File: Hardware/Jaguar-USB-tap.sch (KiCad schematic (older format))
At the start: 24 parts, among them J1 DB15, P1 CONN_01X03, P2 USB_B, P3 CONN_01X05, U1 NCP1117ST33T3G, U2 STM32F070F6, U3 TXB0106, U4 TXB0106, Y1 8MHz

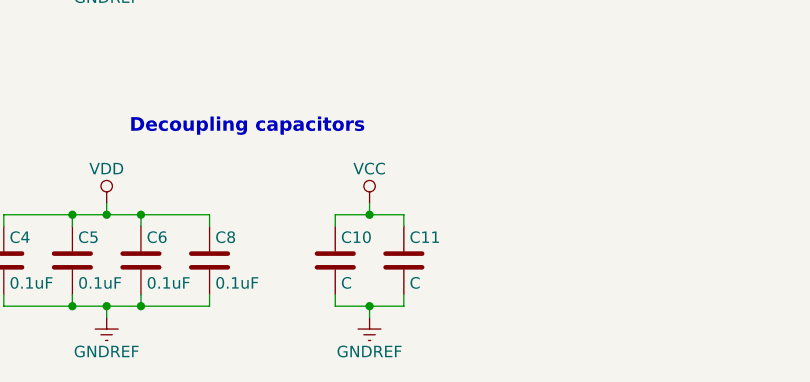
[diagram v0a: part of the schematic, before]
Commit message: Add a preview image for casual inspection.
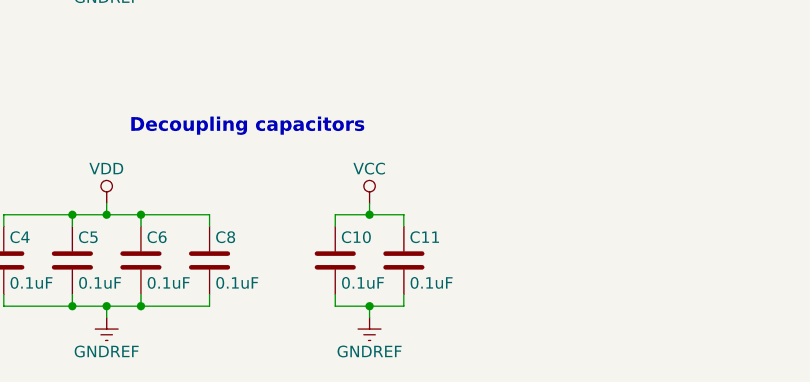
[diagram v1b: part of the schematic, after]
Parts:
- C10, C11: value C -> 0.1uF
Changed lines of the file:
@@
 P 4500 7100
 F 0 "C10" H 4525 7200 50  0000 L CNN
-F 1 "C" H 4525 7000 50  0000 L CNN
+F 1 "0.1uF" H 4525 7000 50  0000 L CNN
 F 2 "" H 4538 6950 50  0000 C CNN
 F 3 "" H 4500 7100 50  0000 C CNN
@@
 P 4800 7100
 F 0 "C11" H 4825 7200 50  0000 L CNN
-F 1 "C" H 4825 7000 50  0000 L CNN
+F 1 "0.1uF" H 4825 7000 50  0000 L CNN
 F 2 "" H 4838 6950 50  0000 C CNN
 F 3 "" H 4800 7100 50  0000 C CNN

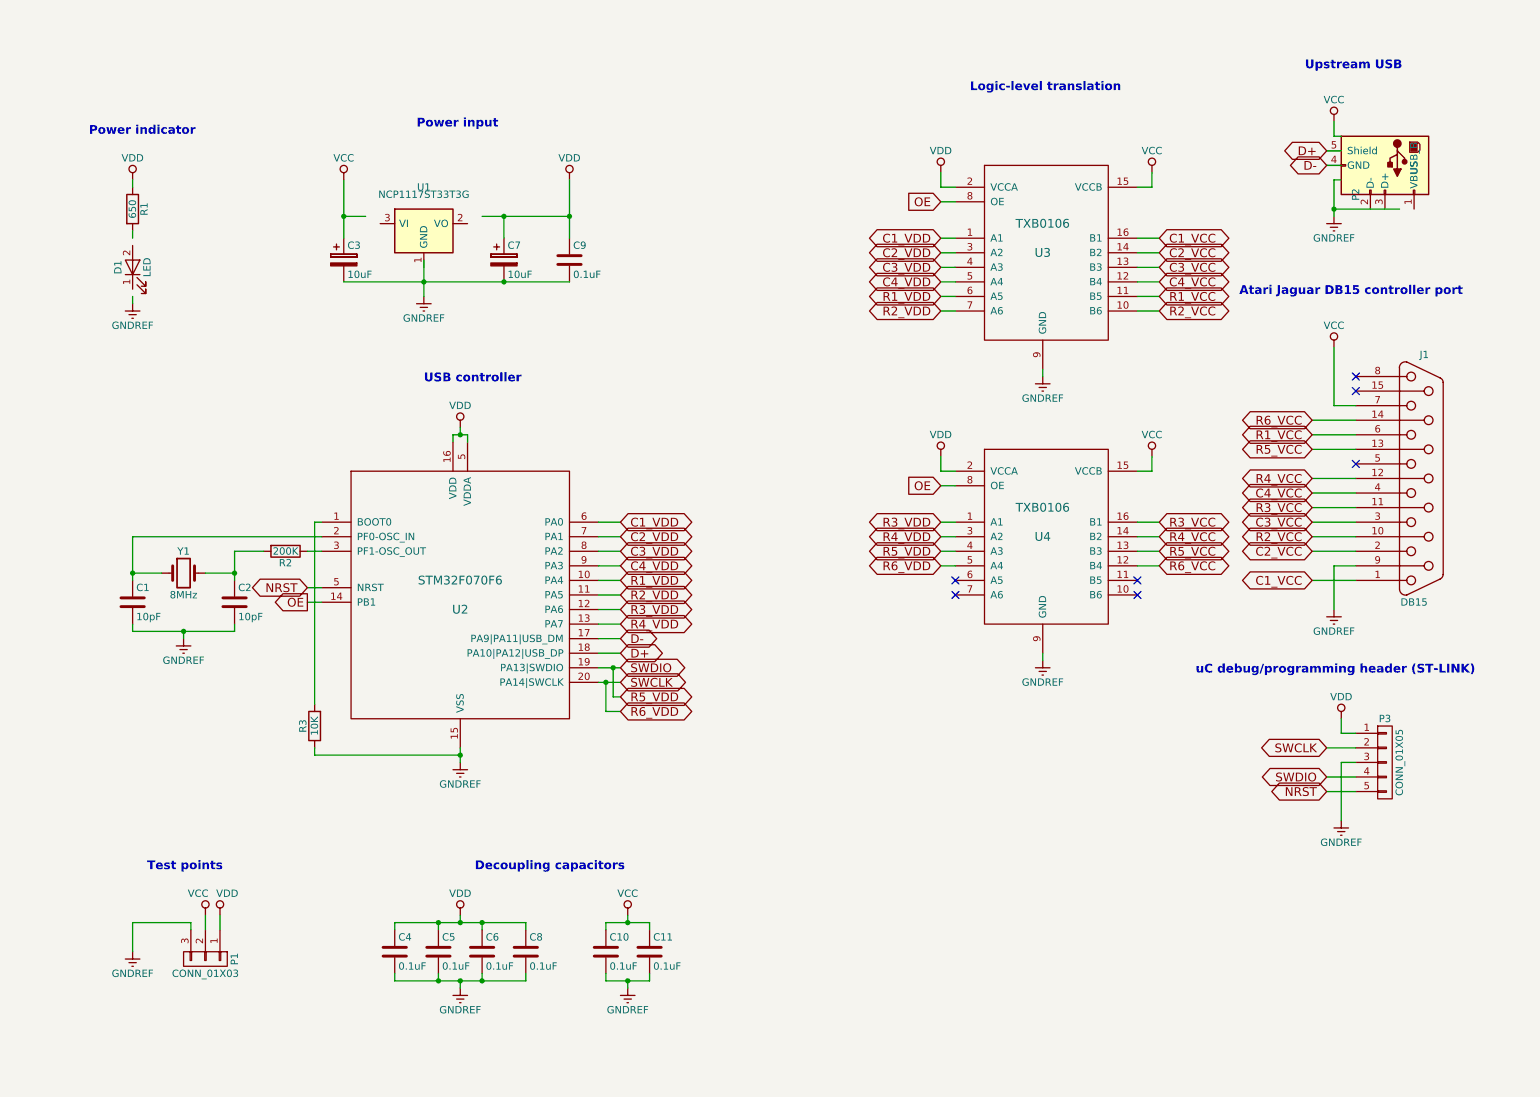
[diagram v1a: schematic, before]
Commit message: Add PCB work.
1) Add footprints for TSSOP16 and TSSOP20 devices.
2) Create a PCB layout for adapter and board cut.
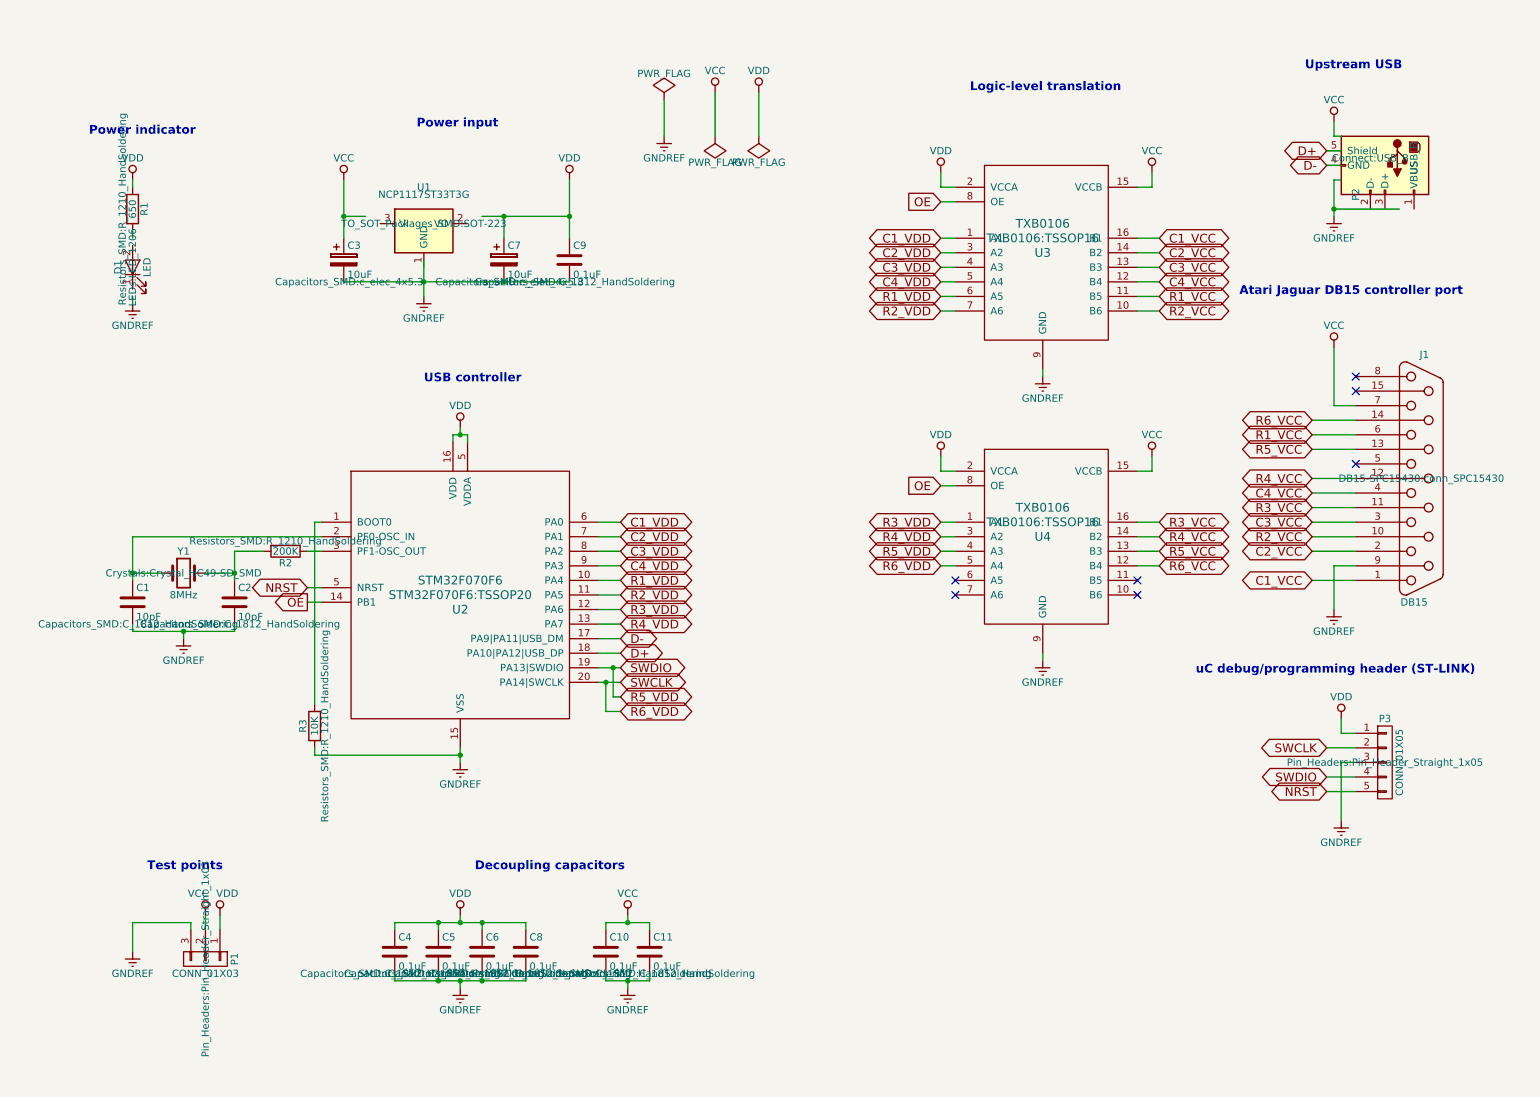
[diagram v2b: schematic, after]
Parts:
- C1, C10, C11, C2, C4, C5, C6, C8, C9: footprint (none) -> Capacitors_SMD:C_1812_HandSoldering
- C3, C7: footprint (none) -> Capacitors_SMD:c_elec_4x5.3
- D1: footprint (none) -> LEDs:LED_1206
- J1: footprint (none) -> DB15-SPC15430:conn_SPC15430
- P1: footprint (none) -> Pin_Headers:Pin_Header_Straight_1x03
- P2: footprint (none) -> Connect:USB_B
- P3: footprint (none) -> Pin_Headers:Pin_Header_Straight_1x05
- R1, R2, R3: footprint (none) -> Resistors_SMD:R_1210_HandSoldering
- U1: footprint (none) -> TO_SOT_Packages_SMD:SOT-223
- U2: footprint (none) -> STM32F070F6:TSSOP20
- U3, U4: footprint (none) -> TXB0106:TSSOP16
- Y1: footprint (none) -> Crystals:Crystal_HC49-SD_SMD
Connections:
- wire segments 133 -> 136
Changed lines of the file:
@@
 F 0 "U2" H 3500 4550 60  0000 C CNN
 F 1 "STM32F070F6" H 3500 4750 60  0000 C CNN
-F 2 "" H 3500 4650 60  0000 C CNN
+F 2 "STM32F070F6:TSSOP20" H 3500 4650 60  0000 C CNN
 F 3 "" H 3500 4650 60  0000 C CNN
 	1    3500 4650
@@
 F 0 "P2" H 10050 1500 50  0000 C CNN
 F 1 "USB_B" H 9800 1900 50  0000 C CNN
-F 2 "" V 9800 1600 50  0000 C CNN
+F 2 "Connect:USB_B" V 9800 1600 50  0000 C CNN
 F 3 "" V 9800 1600 50  0000 C CNN
 	1    9850 1700
@@
 F 0 "P3" H 9850 6100 50  0000 C CNN
 F 1 "CONN_01X05" V 9950 5800 50  0000 C CNN
-F 2 "" H 9850 5800 50  0000 C CNN
+F 2 "Pin_Headers:Pin_Header_Straight_1x05" H 9850 5800 50  0000 C CNN
 F 3 "" H 9850 5800 50  0000 C CNN
 	1    9850 5800
@@
 F 0 "R1" V 1330 2000 50  0000 C CNN
 F 1 "650" V 1250 2000 50  0000 C CNN
-F 2 "" V 1180 2000 50  0000 C CNN
+F 2 "Resistors_SMD:R_1210_HandSoldering" V 1180 2000 50  0000 C CNN
 F 3 "" H 1250 2000 50  0000 C CNN
 	1    1250 2000
@@
 F 0 "D1" H 1250 2500 50  0000 C CNN
 F 1 "LED" H 1250 2300 50  0000 C CNN
-F 2 "" H 1250 2400 50  0000 C CNN
+F 2 "LEDs:LED_1206" H 1250 2400 50  0000 C CNN
 F 3 "" H 1250 2400 50  0000 C CNN
 	1    1250 2400
@@
 F 0 "U1" H 3250 2350 50  0000 C CNN
 F 1 "NCP1117ST33T3G" H 3250 2300 50  0000 C CNN
-F 2 "" H 3250 2100 50  0000 C CNN
+F 2 "TO_SOT_Packages_SMD:SOT-223" H 3250 2100 50  0000 C CNN
 F 3 "" H 3250 2100 50  0000 C CNN
 	1    3250 2100
@@
 F 0 "C3" H 2725 2450 50  0000 L CNN
 F 1 "10uF" H 2725 2250 50  0000 L CNN
-F 2 "" H 2738 2200 50  0000 C CNN
+F 2 "Capacitors_SMD:c_elec_4x5.3" H 2738 2200 50  0000 C CNN
 F 3 "" H 2700 2350 50  0000 C CNN
 	1    2700 2350
@@
 F 0 "C7" H 3825 2450 50  0000 L CNN
 F 1 "10uF" H 3825 2250 50  0000 L CNN
-F 2 "" H 3838 2200 50  0000 C CNN
+F 2 "Capacitors_SMD:c_elec_4x5.3" H 3838 2200 50  0000 C CNN
 F 3 "" H 3800 2350 50  0000 C CNN
 	1    3800 2350
@@
 F 0 "C9" H 4275 2450 50  0000 L CNN
 F 1 "0.1uF" H 4275 2250 50  0000 L CNN
-F 2 "" H 4288 2200 50  0000 C CNN
+F 2 "Capacitors_SMD:C_1812_HandSoldering" H 4288 2200 50  0000 C CNN
 F 3 "" H 4250 2350 50  0000 C CNN
 	1    4250 2350
@@
 F 0 "J1" H 10120 4700 50  0000 C CNN
 F 1 "DB15" H 10050 3000 50  0000 C CNN
-F 2 "" H 10100 3850 50  0000 C CNN
+F 2 "DB15-SPC15430:conn_SPC15430" H 10100 3850 50  0000 C CNN
 F 3 "" H 10100 3850 50  0000 C CNN
 	1    10100 3850
@@
 F 0 "C5" H 3375 7200 50  0000 L CNN
 F 1 "0.1uF" H 3375 7000 50  0000 L CNN
-F 2 "" H 3388 6950 50  0000 C CNN
+F 2 "Capacitors_SMD:C_1812_HandSoldering" H 3388 6950 50  0000 C CNN
 F 3 "" H 3350 7100 50  0000 C CNN
 	1    3350 7100
@@
 F 0 "C6" H 3675 7200 50  0000 L CNN
 F 1 "0.1uF" H 3675 7000 50  0000 L CNN
-F 2 "" H 3688 6950 50  0000 C CNN
+F 2 "Capacitors_SMD:C_1812_HandSoldering" H 3688 6950 50  0000 C CNN
 F 3 "" H 3650 7100 50  0000 C CNN
 	1    3650 7100
@@
 F 0 "R2" V 2380 4350 50  0000 C CNN
 F 1 "200K" V 2300 4350 50  0000 C CNN
-F 2 "" V 2230 4350 50  0000 C CNN
+F 2 "Resistors_SMD:R_1210_HandSoldering" V 2230 4350 50  0000 C CNN
 F 3 "" H 2300 4350 50  0000 C CNN
 	1    2300 4350
@@
 F 0 "Y1" H 1600 4650 50  0000 C CNN
 F 1 "8MHz" H 1600 4350 50  0000 C CNN
-F 2 "" H 1600 4500 50  0000 C CNN
+F 2 "Crystals:Crystal_HC49-SD_SMD" H 1600 4500 50  0000 C CNN
 F 3 "" H 1600 4500 50  0000 C CNN
 	1    1600 4500
@@
 F 0 "C2" H 1975 4800 50  0000 L CNN
 F 1 "10pF" H 1975 4600 50  0000 L CNN
-F 2 "" H 1988 4550 50  0000 C CNN
+F 2 "Capacitors_SMD:C_1812_HandSoldering" H 1988 4550 50  0000 C CNN
 F 3 "" H 1950 4700 50  0000 C CNN
 	1    1950 4700
@@
 F 0 "C1" H 1275 4800 50  0000 L CNN
 F 1 "10pF" H 1275 4600 50  0000 L CNN
-F 2 "" H 1288 4550 50  0000 C CNN
+F 2 "Capacitors_SMD:C_1812_HandSoldering" H 1288 4550 50  0000 C CNN
 F 3 "" H 1250 4700 50  0000 C CNN
 	1    1250 4700
@@
 F 0 "R3" V 2580 5550 50  0000 C CNN
 F 1 "10K" V 2500 5550 50  0000 C CNN
-F 2 "" V 2430 5550 50  0000 C CNN
+F 2 "Resistors_SMD:R_1210_HandSoldering" V 2430 5550 50  0000 C CNN
 F 3 "" H 2500 5550 50  0000 C CNN
 	1    2500 5550
@@
 F 0 "U3" H 7500 2700 60  0000 C CNN
 F 1 "TXB0106" H 7500 2900 60  0000 C CNN
-F 2 "" H 7500 2800 60  0000 C CNN
+F 2 "TXB0106:TSSOP16" H 7500 2800 60  0000 C CNN
 F 3 "" H 7500 2800 60  0000 C CNN
 	1    7500 2500
@@
 F 0 "U4" H 7500 4650 60  0000 C CNN
 F 1 "TXB0106" H 7500 4850 60  0000 C CNN
-F 2 "" H 7500 4750 60  0000 C CNN
+F 2 "TXB0106:TSSOP16" H 7500 4750 60  0000 C CNN
 F 3 "" H 7500 4750 60  0000 C CNN
 	1    7500 4450
@@
 F 0 "C8" H 3975 7200 50  0000 L CNN
 F 1 "0.1uF" H 3975 7000 50  0000 L CNN
-F 2 "" H 3988 6950 50  0000 C CNN
+F 2 "Capacitors_SMD:C_1812_HandSoldering" H 3988 6950 50  0000 C CNN
 F 3 "" H 3950 7100 50  0000 C CNN
 	1    3950 7100
@@
 F 0 "C4" H 3075 7200 50  0000 L CNN
 F 1 "0.1uF" H 3075 7000 50  0000 L CNN
-F 2 "" H 3088 6950 50  0000 C CNN
+F 2 "Capacitors_SMD:C_1812_HandSoldering" H 3088 6950 50  0000 C CNN
 F 3 "" H 3050 7100 50  0000 C CNN
 	1    3050 7100
@@
 F 0 "P1" H 1750 7350 50  0000 C CNN
 F 1 "CONN_01X03" V 1850 7150 50  0000 C CNN
-F 2 "" H 1750 7150 50  0000 C CNN
+F 2 "Pin_Headers:Pin_Header_Straight_1x03" H 1750 7150 50  0000 C CNN
 F 3 "" H 1750 7150 50  0000 C CNN
 	1    1750 7150
@@
 F 0 "C10" H 4525 7200 50  0000 L CNN
 F 1 "0.1uF" H 4525 7000 50  0000 L CNN
-F 2 "" H 4538 6950 50  0000 C CNN
+F 2 "Capacitors_SMD:C_1812_HandSoldering" H 4538 6950 50  0000 C CNN
 F 3 "" H 4500 7100 50  0000 C CNN
 	1    4500 7100
@@
 F 0 "C11" H 4825 7200 50  0000 L CNN
 F 1 "0.1uF" H 4825 7000 50  0000 L CNN
-F 2 "" H 4838 6950 50  0000 C CNN
+F 2 "Capacitors_SMD:C_1812_HandSoldering" H 4838 6950 50  0000 C CNN
 F 3 "" H 4800 7100 50  0000 C CNN
 	1    4800 7100
@@
 Wire Wire Line
 	9350 3450 9650 3450
+$Comp
+L GNDREF #PWR?
+U 1 1 5A144546
+P 4900 1500
+F 0 "#PWR?" H 4900 1250 50  0001 C CNN
+F 1 "GNDREF" H 4900 1350 50  0000 C CNN
+F 2 "" H 4900 1500 50  0000 C CNN
+F 3 "" H 4900 1500 50  0000 C CNN
+	1    4900 1500
+	1    0    0    -1
+$EndComp
+$Comp
+L VCC #PWR?
+U 1 1 5A14458A
+P 5250 1200
+F 0 "#PWR?" H 5250 1050 50  0001 C CNN
+F 1 "VCC" H 5250 1350 50  0000 C CNN
+F 2 "" H 5250 1200 50  0000 C CNN
+F 3 "" H 5250 1200 50  0000 C CNN
+	1    5250 1200
+	1    0    0    -1
+$EndComp
+$Comp
+L VDD #PWR?
+U 1 1 5A1445CE
+P 5550 1200
+F 0 "#PWR?" H 5550 1050 50  0001 C CNN
+F 1 "VDD" H 5550 1350 50  0000 C CNN
+F 2 "" H 5550 1200 50  0000 C CNN
+F 3 "" H 5550 1200 50  0000 C CNN
+	1    5550 1200
+	1    0    0    -1
+$EndComp
+$Comp
+L PWR_FLAG #FLG?
+U 1 1 5A144612
+P 4900 1250
+F 0 "#FLG?" H 4900 1345 50  0001 C CNN
+F 1 "PWR_FLAG" H 4900 1430 50  0000 C CNN
+F 2 "" H 4900 1250 50  0000 C CNN
+F 3 "" H 4900 1250 50  0000 C CNN
+	1    4900 1250
+	1    0    0    -1
+$EndComp
+$Comp
+L PWR_FLAG #FLG?
+U 1 1 5A1446FA
+P 5250 1500
+F 0 "#FLG?" H 5250 1595 50  0001 C CNN
+F 1 "PWR_FLAG" H 5250 1680 50  0000 C CNN
+F 2 "" H 5250 1500 50  0000 C CNN
+F 3 "" H 5250 1500 50  0000 C CNN
+	1    5250 1500
+	-1   0    0    1
+$EndComp
+$Comp
+L PWR_FLAG #FLG?
+U 1 1 5A14473E
+P 5550 1500
+F 0 "#FLG?" H 5550 1595 50  0001 C CNN
+F 1 "PWR_FLAG" H 5550 1680 50  0000 C CNN
+F 2 "" H 5550 1500 50  0000 C CNN
+F 3 "" H 5550 1500 50  0000 C CNN
+	1    5550 1500
+	-1   0    0    1
+$EndComp
+Wire Wire Line
+	4900 1500 4900 1250
+Wire Wire Line
+	5250 1200 5250 1500
+Wire Wire Line
+	5550 1200 5550 1500
 $EndSCHEMATC
